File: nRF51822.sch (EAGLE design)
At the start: 14 parts

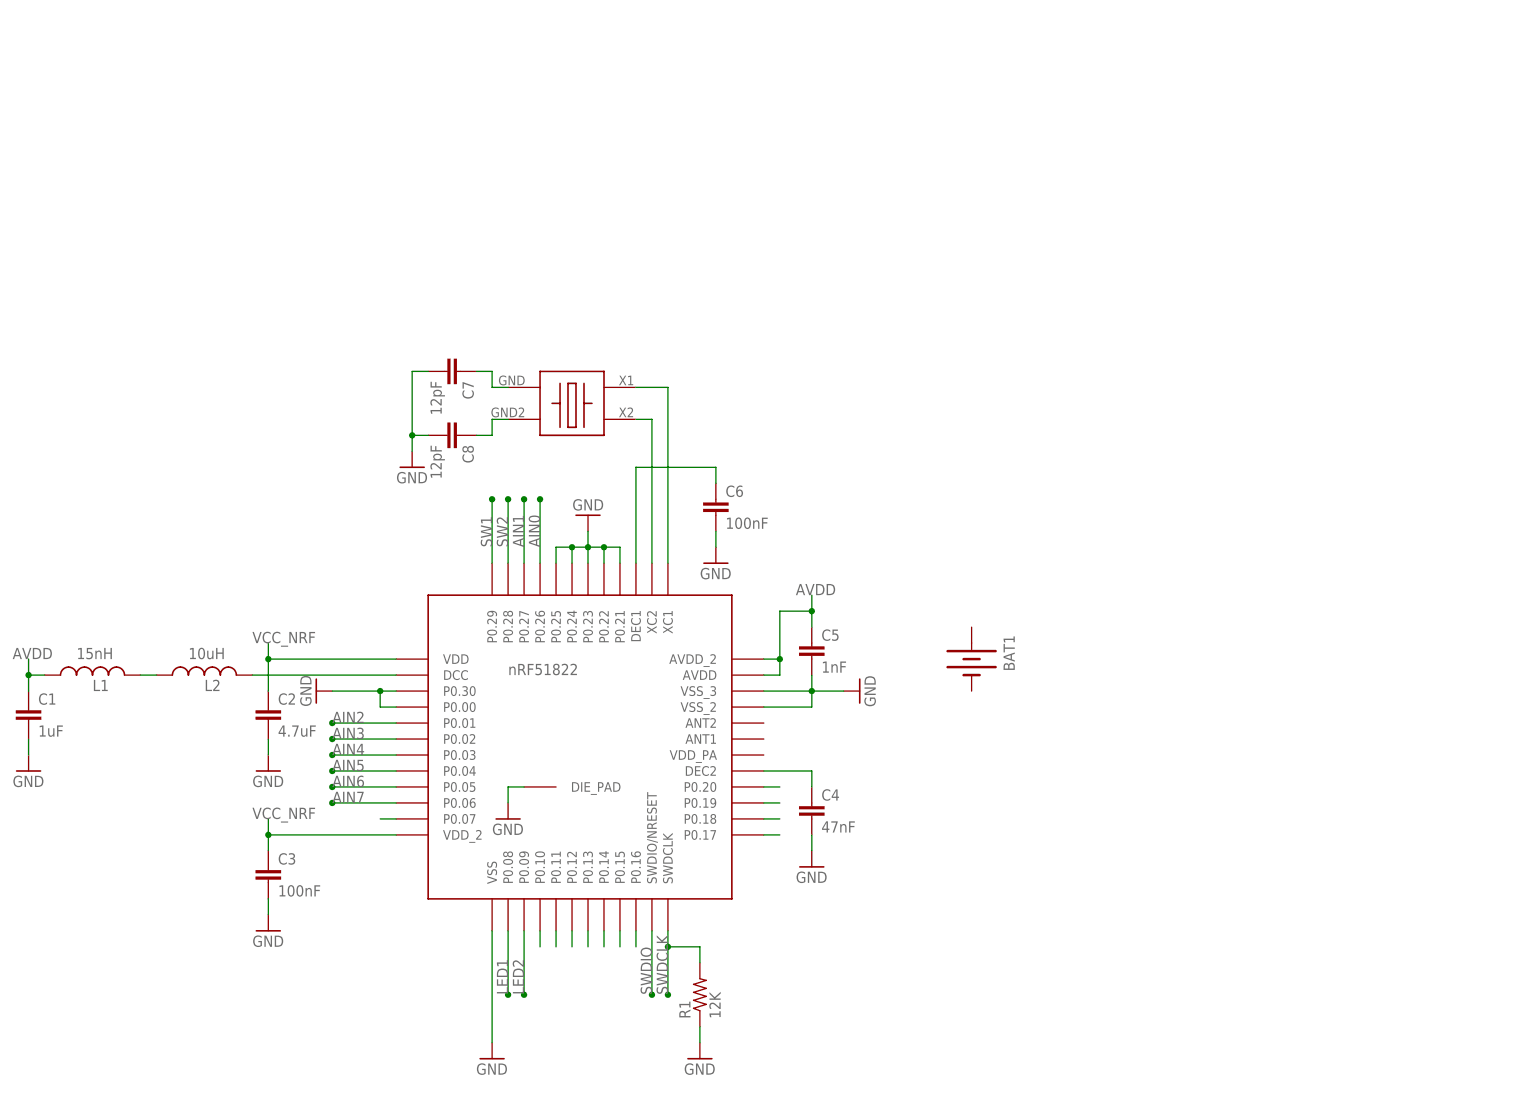
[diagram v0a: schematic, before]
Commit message: Agregado de mas modulos
Agregado Leds, Switchs y Alimentación
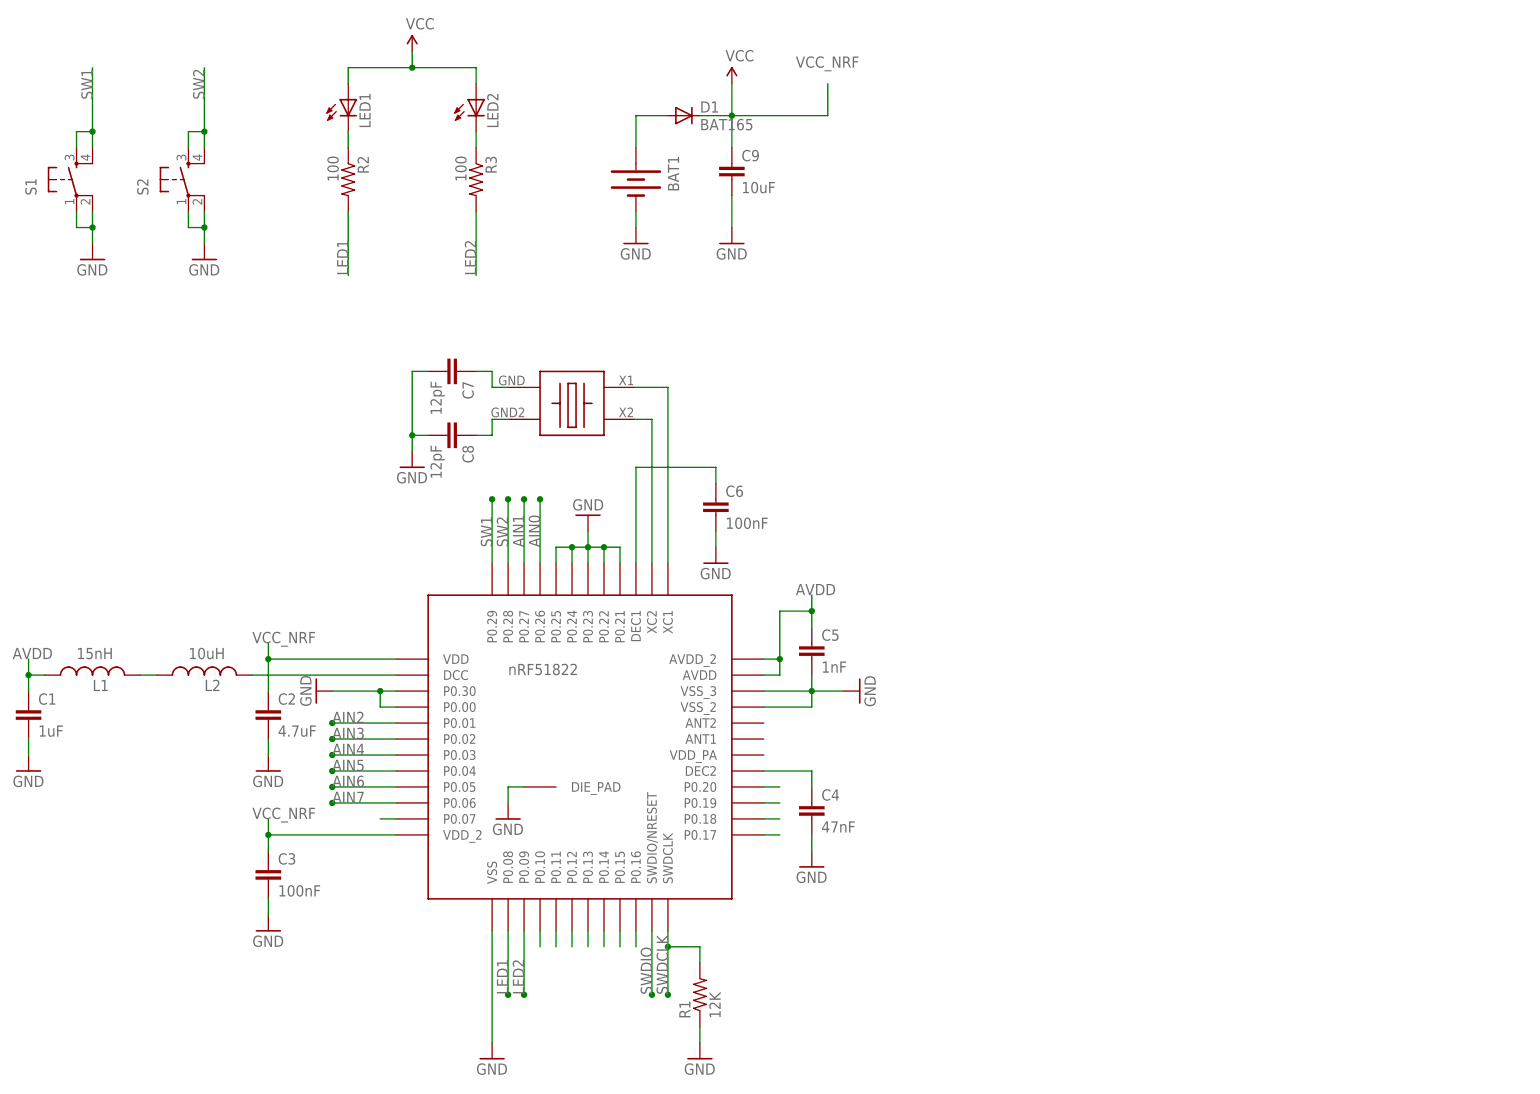
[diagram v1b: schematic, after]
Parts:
- added C9: 10uF, SparkFun-Capacitors:CAP0603-CAP
- added D1: BAT165, SparkFun-DiscreteSemi:DIODESOD
- added LED1, LED2: (no value), SparkFun-LED:LED0603
- added R2, R3: 100, SparkFun-Resistors:RESISTOR0603-RES
- added S1, S2: (no value), SparkFun-Electromechanical:TAC_SWITCHSMD
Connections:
- new net N$16: BAT1.+, D1.A
- new net N$18: LED2.C, R3.1
- new net N$19: LED1.C, R2.1
- new net VCC: LED1.A, LED2.A
- net GND: now also BAT1.-, C9.2, S1.1, S1.2, S2.1, S2.2
- net LED1: now also R2.2
- net LED2: now also R3.2
- net SW1: now also S1.3, S1.4
- net SW2: now also S2.3, S2.4
- net VCC_NRF: now also C9.1, D1.C
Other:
- note added: "ANTENNA"
- note added: "CONNECTORS"
- note added: "LEDS"
- note added: "POWER"
- note added: "RADIO"
- note added: "SWITCH"
- note removed: "Radio"
- moved on the sheet: BAT1

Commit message: Update BOM
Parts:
- added JP1, JP2: M05X2SHD_SMD, SparkFun-Connectors:M05X2SHD_SMD
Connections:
- new net N$17: JP2.4
- new net N$20: JP2.3
- new net N$21: JP2.5
- new net N$22: JP2.7
- new net N$23: JP2.9
- new net N$24: JP2.6
- new net N$25: JP2.8
- new net N$26: JP2.10
- net GND: now also JP1.3, JP1.5, JP1.9, JP2.2
- net SWDCLK: now also JP1.4
- net SWDIO: now also JP1.2
- net VCC: now also JP1.1, JP2.1
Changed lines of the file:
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@@
 <part name="GND14" library="SparkFun-Aesthetics" deviceset="GND" device=""/>
 <part name="GND16" library="SparkFun-Aesthetics" deviceset="GND" device=""/>
+<part name="JP1" library="SparkFun-Connectors" deviceset="M05X2" device="SHD_SMD"/>
+<part name="SUPPLY3" library="SparkFun-Aesthetics" deviceset="VCC" device=""/>
+<part name="GND17" library="SparkFun-Aesthetics" deviceset="GND" device=""/>
+<part name="JP2" library="SparkFun-Connectors" deviceset="M05X2" device="SHD_SMD"/>
+<part name="SUPPLY4" library="SparkFun-Aesthetics" deviceset="VCC" device=""/>
+<part name="GND18" library="SparkFun-Aesthetics" deviceset="GND" device=""/>
 </parts>
 <sheets>
@@
 <instance part="GND14" gate="1" x="17.78" y="134.62"/>
 <instance part="GND16" gate="1" x="35.56" y="134.62"/>
+<instance part="JP1" gate="G$1" x="165.1" y="157.48"/>
+<instance part="SUPPLY3" gate="1" x="152.4" y="165.1"/>
+<instance part="GND17" gate="1" x="152.4" y="144.78"/>
+<instance part="JP2" gate="G$1" x="215.9" y="157.48"/>
+<instance part="SUPPLY4" gate="1" x="203.2" y="165.1"/>
+<instance part="GND18" gate="1" x="228.6" y="167.64" rot="R180"/>
 </instances>
 <busses>
@@
 <junction x="35.56" y="139.7"/>
 </segment>
+<segment>
+<pinref part="JP1" gate="G$1" pin="9"/>
+<pinref part="GND17" gate="1" pin="GND"/>
+<wire x1="157.48" y1="152.4" x2="152.4" y2="152.4" width="0.1524" layer="91"/>
+<wire x1="152.4" y1="152.4" x2="152.4" y2="147.32" width="0.1524" layer="91"/>
+<pinref part="JP1" gate="G$1" pin="5"/>
+<wire x1="157.48" y1="157.48" x2="152.4" y2="157.48" width="0.1524" layer="91"/>
+<wire x1="152.4" y1="157.48" x2="152.4" y2="152.4" width="0.1524" layer="91"/>
+<junction x="152.4" y="152.4"/>
+<pinref part="JP1" gate="G$1" pin="3"/>
+<wire x1="157.48" y1="160.02" x2="152.4" y2="160.02" width="0.1524" layer="91"/>
+<wire x1="152.4" y1="160.02" x2="152.4" y2="157.48" width="0.1524" layer="91"/>
+<junction x="152.4" y="157.48"/>
+</segment>
+<segment>
+<pinref part="JP2" gate="G$1" pin="2"/>
+<pinref part="GND18" gate="1" pin="GND"/>
+<wire x1="223.52" y1="162.56" x2="228.6" y2="162.56" width="0.1524" layer="91"/>
+<wire x1="228.6" y1="162.56" x2="228.6" y2="165.1" width="0.1524" layer="91"/>
+</segment>
 </net>
 <net name="SWDCLK" class="0">
@@
 <junction x="109.22" y="17.78"/>
 </segment>
+<segment>
+<pinref part="JP1" gate="G$1" pin="4"/>
+<wire x1="172.72" y1="160.02" x2="185.42" y2="160.02" width="0.1524" layer="91"/>
+<label x="175.26" y="160.02" size="1.778" layer="95"/>
+</segment>
 </net>
 <net name="LED1" class="0">
@@
 <label x="106.68" y="17.78" size="1.778" layer="95" rot="R90"/>
 <junction x="106.68" y="17.78"/>
+</segment>
+<segment>
+<pinref part="JP1" gate="G$1" pin="2"/>
+<wire x1="172.72" y1="162.56" x2="185.42" y2="162.56" width="0.1524" layer="91"/>
+<label x="175.26" y="162.56" size="1.778" layer="95"/>
 </segment>
 </net>
@@
 <junction x="68.58" y="165.1"/>
 </segment>
+<segment>
+<pinref part="JP1" gate="G$1" pin="1"/>
+<pinref part="SUPPLY3" gate="1" pin="VCC"/>
+<wire x1="157.48" y1="162.56" x2="152.4" y2="162.56" width="0.1524" layer="91"/>
+<wire x1="152.4" y1="162.56" x2="152.4" y2="165.1" width="0.1524" layer="91"/>
+</segment>
+<segment>
+<pinref part="JP2" gate="G$1" pin="1"/>
+<pinref part="SUPPLY4" gate="1" pin="VCC"/>
+<wire x1="208.28" y1="162.56" x2="203.2" y2="162.56" width="0.1524" layer="91"/>
+<wire x1="203.2" y1="162.56" x2="203.2" y2="165.1" width="0.1524" layer="91"/>
+</segment>
 </net>
 <net name="N$18" class="0">
@@
 </segment>
 </net>
+<net name="N$17" class="0">
+<segment>
+<pinref part="JP2" gate="G$1" pin="4"/>
+<wire x1="223.52" y1="160.02" x2="231.14" y2="160.02" width="0.1524" layer="91"/>
+<label x="226.06" y="160.02" size="1.778" layer="95"/>
+</segment>
+</net>
+<net name="N$20" class="0">
+<segment>
+<pinref part="JP2" gate="G$1" pin="3"/>
+<wire x1="208.28" y1="160.02" x2="200.66" y2="160.02" width="0.1524" layer="91"/>
+<label x="200.66" y="160.02" size="1.778" layer="95"/>
+</segment>
+</net>
+<net name="N$21" class="0">
+<segment>
+<pinref part="JP2" gate="G$1" pin="5"/>
+<wire x1="208.28" y1="157.48" x2="200.66" y2="157.48" width="0.1524" layer="91"/>
+<label x="200.66" y="157.48" size="1.778" layer="95"/>
+</segment>
+</net>
+<net name="N$22" class="0">
+<segment>
+<pinref part="JP2" gate="G$1" pin="7"/>
+<wire x1="208.28" y1="154.94" x2="200.66" y2="154.94" width="0.1524" layer="91"/>
+<label x="200.66" y="154.94" size="1.778" layer="95"/>
+</segment>
+</net>
+<net name="N$23" class="0">
+<segment>
+<pinref part="JP2" gate="G$1" pin="9"/>
+<wire x1="208.28" y1="152.4" x2="200.66" y2="152.4" width="0.1524" layer="91"/>
+<label x="200.66" y="152.4" size="1.778" layer="95"/>
+</segment>
+</net>
+<net name="N$24" class="0">
+<segment>
+<pinref part="JP2" gate="G$1" pin="6"/>
+<wire x1="223.52" y1="157.48" x2="231.14" y2="157.48" width="0.1524" layer="91"/>
+<label x="226.06" y="157.48" size="1.778" layer="95"/>
+</segment>
+</net>
+<net name="N$25" class="0">
+<segment>
+<pinref part="JP2" gate="G$1" pin="8"/>
+<wire x1="223.52" y1="154.94" x2="231.14" y2="154.94" width="0.1524" layer="91"/>
+<label x="226.06" y="154.94" size="1.778" layer="95"/>
+</segment>
+</net>
+<net name="N$26" class="0">
+<segment>
+<pinref part="JP2" gate="G$1" pin="10"/>
+<wire x1="223.52" y1="152.4" x2="231.14" y2="152.4" width="0.1524" layer="91"/>
+<label x="226.06" y="152.4" size="1.778" layer="95"/>
+</segment>
+</net>

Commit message: Terminado el Esquemático
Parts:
- added C10, C11: 0.1uF, SparkFun-Capacitors:CAP0603-CAP
- added C12: 2.2nF, SparkFun-Capacitors:CAP0603-CAP
- added U$3: BALUN-2450BM, NordicSemi:BALUN-2450BM
- added U$4: ANTENA-2450AT, NordicSemi:ANTENA-2450AT
- JP1: value M05X2SHD_SMD -> PROG-JLINK-SEAGGER; device SparkFun-Connectors:M05X2SHD_SMD -> NordicSemi:PROG-JLINK-SEAGGER
- JP2: value M05X2SHD_SMD -> PIN_HEADER_IO; device SparkFun-Connectors:M05X2SHD_SMD -> NordicSemi:PIN_HEADER_IO
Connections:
- removed net N$17: JP2.4
- removed net N$20: JP2.3
- removed net N$21: JP2.5
- removed net N$23: JP2.9
- removed net N$24: JP2.6
- removed net N$25: JP2.8
- removed net N$26: JP2.10
- new net ANT1: U$1.ANT1, U$3.BAL2
- new net ANT2: U$1.ANT2, U$3.BAL1
- new net SDWCLK: JP1.SWDCLK
- new net VDD_PA: C12.1, U$1.VDD_PA, U$3.DC
- net AIN0: now also JP2.3
- net AIN1: now also JP2.5
- net AIN2: now also JP2.7
- net AIN3: now also JP2.9
- net AIN4: now also JP2.10
- net AIN5: now also JP2.8
- net AIN6: now also JP2.6
- net AIN7: now also JP2.4
- net GND: now also C10.2, C11.2, C12.2, JP1.GND, JP1.GND1, JP1.GND2, U$3.GND; no longer JP1.3, JP1.5, JP1.9
- net N$22: now also U$3.UNBL, U$4.FP; no longer JP2.7
- net SWDCLK: no longer JP1.4
- net SWDIO: now also JP1.SWDIO; no longer JP1.2
- net VCC: now also C10.1, C11.1, JP1.VCC; no longer JP1.1
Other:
- moved on the sheet: JP1, JP2

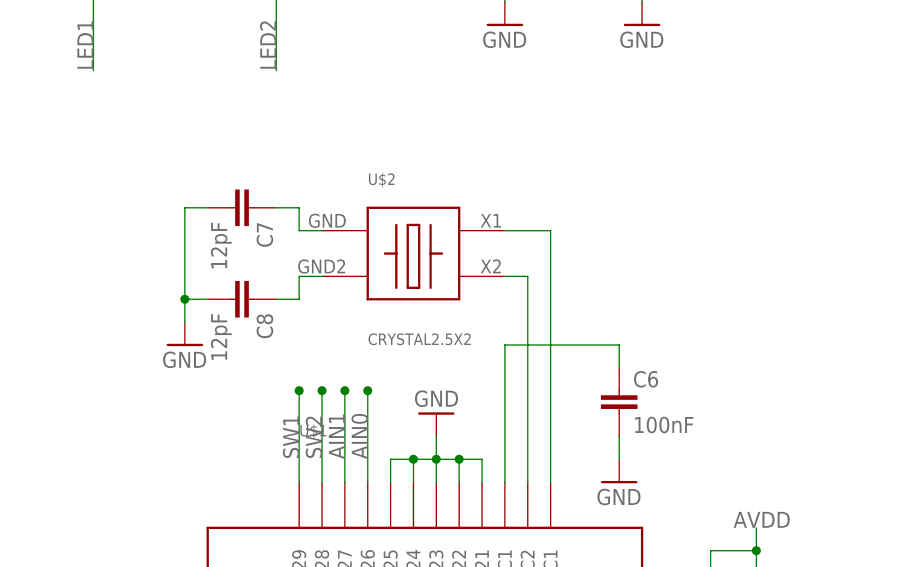
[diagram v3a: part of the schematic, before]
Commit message: Correccion Capacitores
Correccion de los capacitores C1 y C2 del Crystal
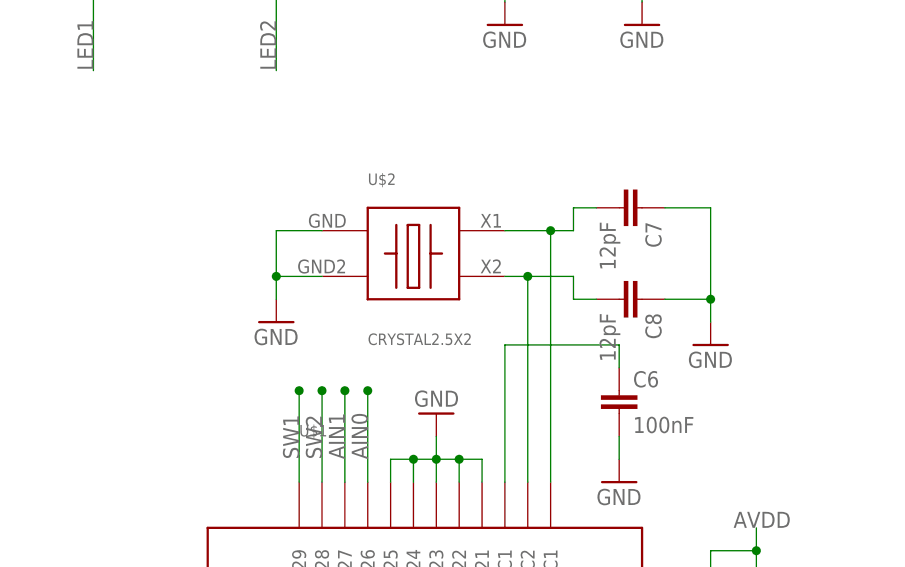
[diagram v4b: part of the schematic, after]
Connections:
- removed net N$7: C8.1, U$2.GND2
- removed net N$9: C7.1, U$2.GND
- net GND: now also C7.1, C8.1, U$2.GND, U$2.GND2; no longer C7.2, C8.2
- net N$4: now also C8.2
- net N$5: now also C7.2
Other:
- moved on the sheet: C7, C8
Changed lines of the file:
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@@
 <setting verticaltext="up"/>
 </settings>
-<grid distance="0.1" unitdist="inch" unit="inch" style="lines" multiple="1" display="yes" altdistance="0.01" altunitdist="inch" altunit="inch"/>
+<grid distance="0.1" unitdist="inch" unit="inch" style="lines" multiple="1" display="no" altdistance="0.01" altunitdist="inch" altunit="inch"/>
 <layers>
 <layer number="1" name="Top" color="4" fill="1" visible="no" active="no"/>
@@
 <part name="GND20" library="SparkFun-Aesthetics" deviceset="GND" device=""/>
 <part name="GND21" library="SparkFun-Aesthetics" deviceset="GND" device=""/>
+<part name="GND22" library="SparkFun-Aesthetics" deviceset="GND" device=""/>
 </parts>
 <sheets>
@@
 <instance part="C6" gate="G$1" x="116.84" y="93.98"/>
 <instance part="GND11" gate="1" x="116.84" y="86.36"/>
-<instance part="C7" gate="G$1" x="73.66" y="116.84" rot="R270"/>
-<instance part="C8" gate="G$1" x="73.66" y="106.68" rot="R270"/>
-<instance part="GND13" gate="1" x="68.58" y="101.6"/>
+<instance part="C7" gate="G$1" x="116.84" y="116.84" rot="R270"/>
+<instance part="C8" gate="G$1" x="116.84" y="106.68" rot="R270"/>
+<instance part="GND13" gate="1" x="78.74" y="104.14"/>
 <instance part="U$2" gate="G$1" x="93.98" y="111.76"/>
 <instance part="BAT1" gate="G$1" x="104.14" y="147.32" rot="R270"/>
@@
 <instance part="GND20" gate="1" x="185.42" y="50.8"/>
 <instance part="GND21" gate="1" x="185.42" y="99.06" rot="R180"/>
+<instance part="GND22" gate="1" x="127" y="101.6"/>
 </instances>
 <busses>
@@
 </segment>
 <segment>
-<pinref part="C7" gate="G$1" pin="2"/>
-<pinref part="GND13" gate="1" pin="GND"/>
-<wire x1="71.12" y1="116.84" x2="68.58" y2="116.84" width="0.1524" layer="91"/>
-<wire x1="68.58" y1="116.84" x2="68.58" y2="106.68" width="0.1524" layer="91"/>
-<pinref part="C8" gate="G$1" pin="2"/>
-<wire x1="68.58" y1="106.68" x2="68.58" y2="104.14" width="0.1524" layer="91"/>
-<wire x1="71.12" y1="106.68" x2="68.58" y2="106.68" width="0.1524" layer="91"/>
-<junction x="68.58" y="106.68"/>
-</segment>
-<segment>
 <pinref part="BAT1" gate="G$1" pin="-"/>
 <pinref part="GND12" gate="1" pin="GND"/>
@@
 <wire x1="185.42" y1="91.44" x2="185.42" y2="96.52" width="0.1524" layer="91"/>
 </segment>
+<segment>
+<pinref part="U$2" gate="G$1" pin="GND2"/>
+<pinref part="GND13" gate="1" pin="GND"/>
+<wire x1="78.74" y1="106.68" x2="78.74" y2="109.22" width="0.1524" layer="91"/>
+<wire x1="78.74" y1="109.22" x2="83.82" y2="109.22" width="0.1524" layer="91"/>
+<pinref part="U$2" gate="G$1" pin="GND"/>
+<wire x1="83.82" y1="114.3" x2="78.74" y2="114.3" width="0.1524" layer="91"/>
+<wire x1="78.74" y1="114.3" x2="78.74" y2="109.22" width="0.1524" layer="91"/>
+<junction x="78.74" y="109.22"/>
+</segment>
+<segment>
+<pinref part="C8" gate="G$1" pin="1"/>
+<pinref part="GND22" gate="1" pin="GND"/>
+<wire x1="121.92" y1="106.68" x2="127" y2="106.68" width="0.1524" layer="91"/>
+<wire x1="127" y1="106.68" x2="127" y2="104.14" width="0.1524" layer="91"/>
+<pinref part="C7" gate="G$1" pin="1"/>
+<wire x1="121.92" y1="116.84" x2="127" y2="116.84" width="0.1524" layer="91"/>
+<wire x1="127" y1="116.84" x2="127" y2="106.68" width="0.1524" layer="91"/>
+<junction x="127" y="106.68"/>
+</segment>
 </net>
 <net name="SWDCLK" class="0">
@@
 <wire x1="106.68" y1="86.36" x2="106.68" y2="109.22" width="0.1524" layer="91"/>
 <wire x1="106.68" y1="109.22" x2="104.14" y2="109.22" width="0.1524" layer="91"/>
+<pinref part="C8" gate="G$1" pin="2"/>
+<wire x1="114.3" y1="106.68" x2="111.76" y2="106.68" width="0.1524" layer="91"/>
+<wire x1="111.76" y1="106.68" x2="111.76" y2="109.22" width="0.1524" layer="91"/>
+<wire x1="111.76" y1="109.22" x2="106.68" y2="109.22" width="0.1524" layer="91"/>
+<junction x="106.68" y="109.22"/>
 </segment>
 </net>
@@
 <wire x1="109.22" y1="86.36" x2="109.22" y2="114.3" width="0.1524" layer="91"/>
 <wire x1="109.22" y1="114.3" x2="104.14" y2="114.3" width="0.1524" layer="91"/>
-</segment>
-</net>
-<net name="N$7" class="0">
-<segment>
-<pinref part="U$2" gate="G$1" pin="GND2"/>
-<wire x1="83.82" y1="109.22" x2="81.28" y2="109.22" width="0.1524" layer="91"/>
-<pinref part="C8" gate="G$1" pin="1"/>
-<wire x1="81.28" y1="109.22" x2="81.28" y2="106.68" width="0.1524" layer="91"/>
-<wire x1="81.28" y1="106.68" x2="78.74" y2="106.68" width="0.1524" layer="91"/>
-</segment>
-</net>
-<net name="N$9" class="0">
-<segment>
-<pinref part="U$2" gate="G$1" pin="GND"/>
-<wire x1="83.82" y1="114.3" x2="81.28" y2="114.3" width="0.1524" layer="91"/>
-<pinref part="C7" gate="G$1" pin="1"/>
-<wire x1="81.28" y1="114.3" x2="81.28" y2="116.84" width="0.1524" layer="91"/>
-<wire x1="81.28" y1="116.84" x2="78.74" y2="116.84" width="0.1524" layer="91"/>
-</segment>
-</net>
+<pinref part="C7" gate="G$1" pin="2"/>
+<wire x1="114.3" y1="116.84" x2="111.76" y2="116.84" width="0.1524" layer="91"/>
+<wire x1="111.76" y1="116.84" x2="111.76" y2="114.3" width="0.1524" layer="91"/>
+<wire x1="111.76" y1="114.3" x2="109.22" y2="114.3" width="0.1524" layer="91"/>
+<junction x="109.22" y="114.3"/>
+</segment>
+</net>
